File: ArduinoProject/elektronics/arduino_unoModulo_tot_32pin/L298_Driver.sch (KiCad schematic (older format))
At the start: 6 parts, among them U301 74AHC1G04, U302 L298D, U303 74AHC1G04

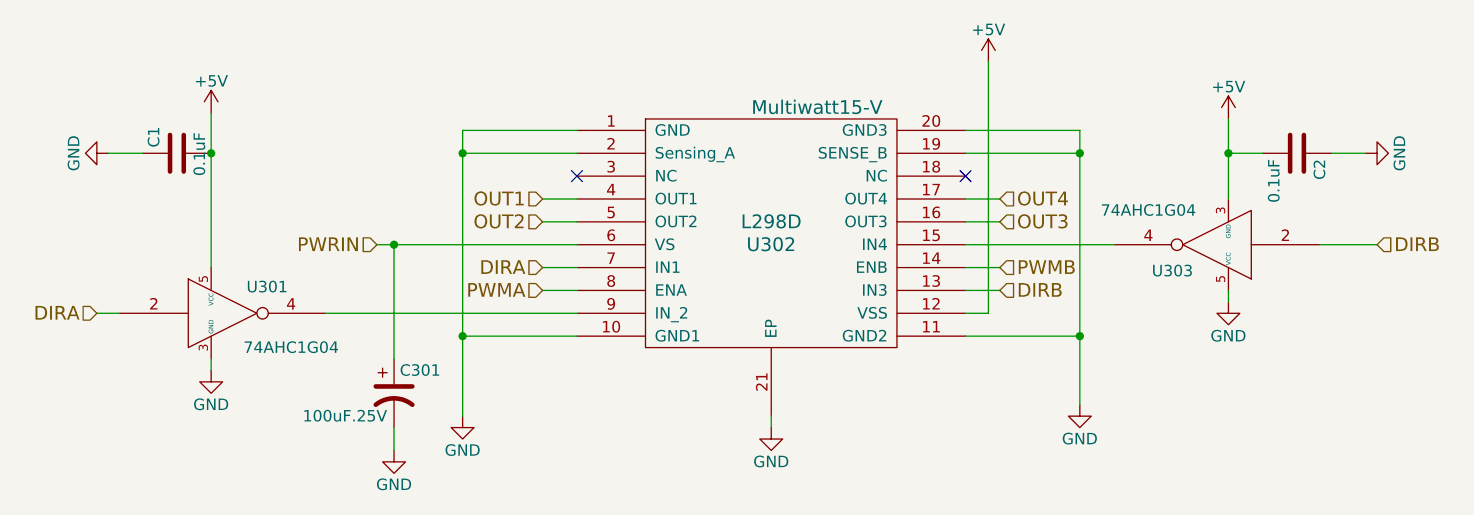
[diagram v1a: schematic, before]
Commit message: arduino routed
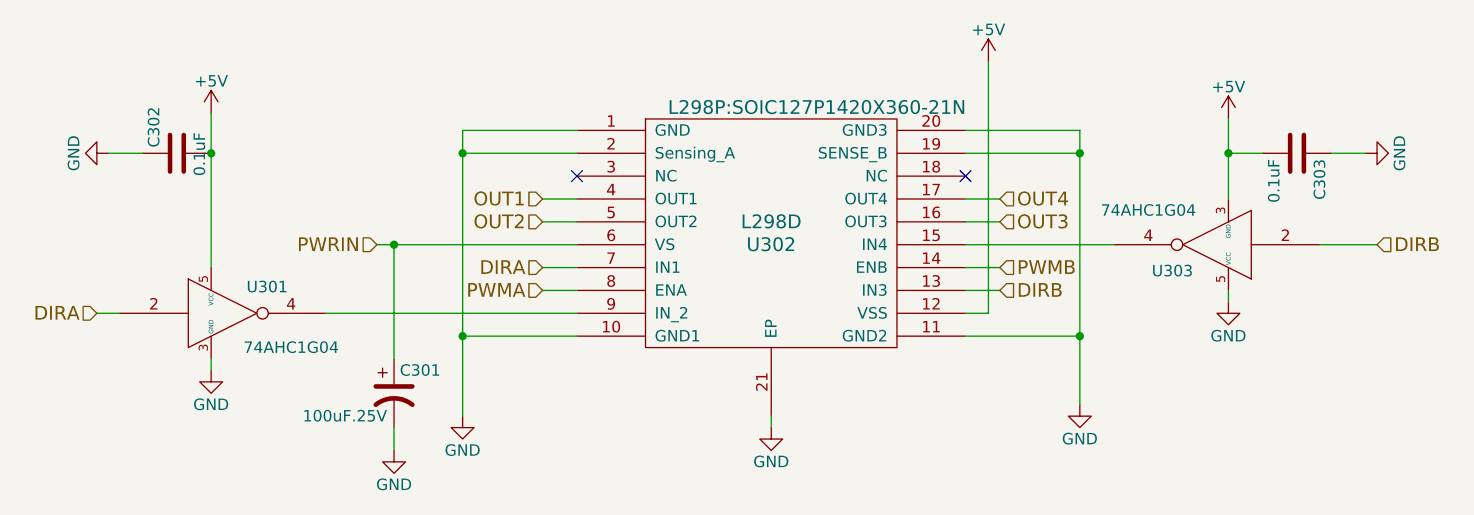
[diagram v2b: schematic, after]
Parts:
- U301, U303: footprint (none) -> 74AHC1G04SE-7:SOT65P210X110-5N
- U302: footprint Multiwatt15-V -> L298P:SOIC127P1420X360-21N
- renumbered C1 to C302, C2 to C303
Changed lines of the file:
@@
 F 0 "U302" H 5800 3000 60  0000 C CNN
 F 1 "L298D" H 5800 3100 60  0000 C CNN
-F 2 "Multiwatt15-V" H 6000 3600 60  0000 C CNN
+F 2 "L298P:SOIC127P1420X360-21N" H 6000 3600 60  0000 C CNN
 F 3 "" H 5800 3000 60  0001 C CNN
 	1    5800 3000
@@
 F 0 "U301" H 3595 3415 50  0000 C CNN
 F 1 "74AHC1G04" H 3700 3150 50  0000 C CNN
-F 2 "" H 3400 3300 50  0001 C CNN
+F 2 "74AHC1G04SE-7:SOT65P210X110-5N" H 3400 3300 50  0001 C CNN
 F 3 "" H 3400 3300 50  0001 C CNN
 	1    3400 3300
@@
 F 0 "U303" H 7945 3115 50  0000 C CNN
 F 1 "74AHC1G04" H 8050 2850 50  0000 C CNN
-F 2 "" H 7750 3000 50  0001 C CNN
+F 2 "74AHC1G04SE-7:SOT65P210X110-5N" H 7750 3000 50  0001 C CNN
 F 3 "" H 7750 3000 50  0001 C CNN
 	1    7750 3000
@@
 $EndComp
 $Comp
-L C C2
+L C C303
 U 1 1 5A9642A9
 P 8100 2600
-F 0 "C2" H 8125 2700 50  0000 L CNN
+F 0 "C303" H 8125 2700 50  0000 L CNN
 F 1 "0.1uF" H 8125 2500 50  0000 L CNN
 F 2 "Capacitors_SMD:C_0805" H 8138 2450 50  0001 C CNN
@@
 $EndComp
 $Comp
-L C C1
+L C C302
 U 1 1 5A9647F3
 P 3200 2600
-F 0 "C1" H 3225 2700 50  0000 L CNN
+F 0 "C302" H 3225 2700 50  0000 L CNN
 F 1 "0.1uF" H 3100 2500 50  0000 L CNN
 F 2 "Capacitors_SMD:C_0805" H 3238 2450 50  0001 C CNN

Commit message: arduino routint altered2
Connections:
- net OUT3: now also U302.17 (OUT4); no longer U302.16 (OUT3)
- net OUT4: now also U302.16 (OUT3); no longer U302.17 (OUT4)
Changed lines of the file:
@@
 OUT2
 Text HLabel 6800 2900 2    60   Input ~ 0
+OUT4
+Text HLabel 6800 2800 2    60   Input ~ 0
 OUT3
-Text HLabel 6800 2800 2    60   Input ~ 0
-OUT4
 Text HLabel 6800 3100 2    60   Input ~ 0
 PWMB
